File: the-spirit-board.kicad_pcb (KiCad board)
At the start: 4 copper layers, 25 x 43 mm, 60 parts, among them IC1 ESP32-C6-WROOM-1-N8, IC2 AP2112K-3.3TRG1, IC3 ICS-43434, J1 RAHUC31AUTR, Q1 BSS138, Q2 BSS138, Q3 BSS138, Q4 BSS138, Q5 BSS138, Q6 BSS138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

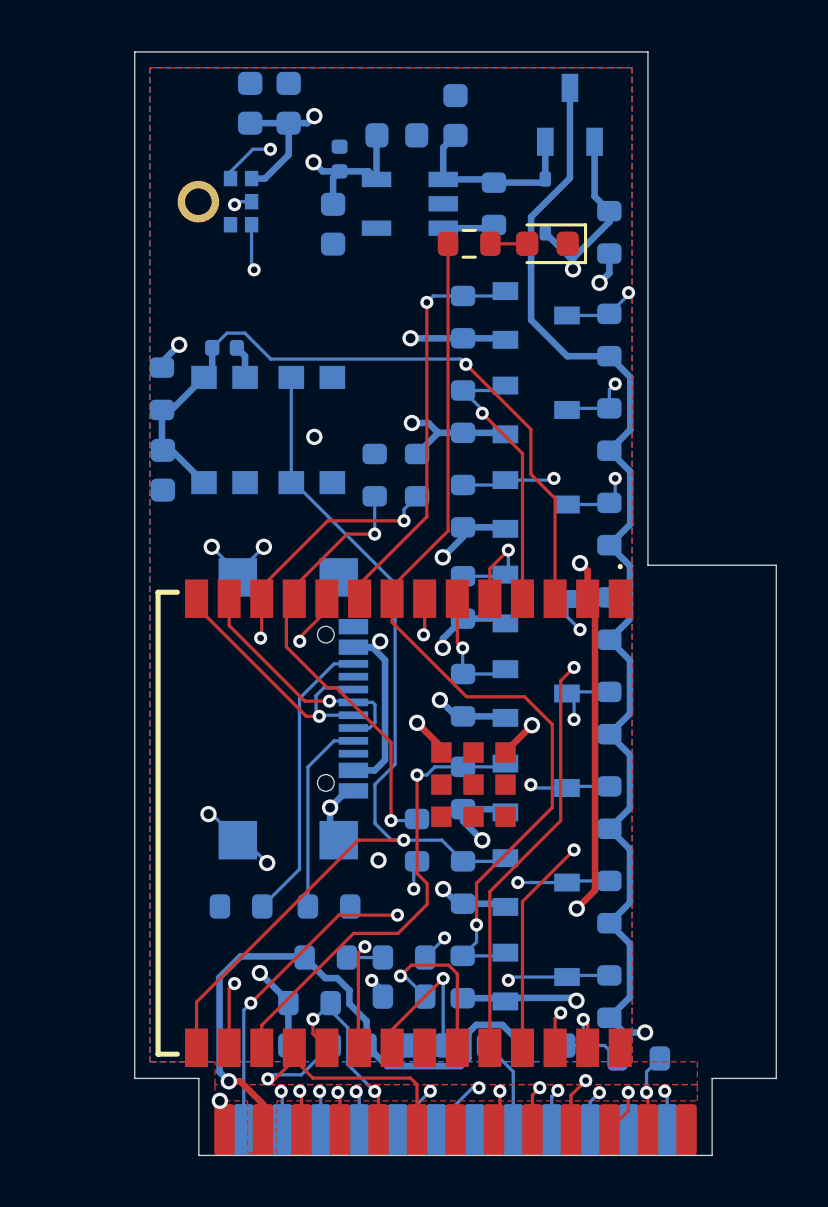
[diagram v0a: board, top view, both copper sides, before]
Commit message: Update the schematic and layout after choosing parts
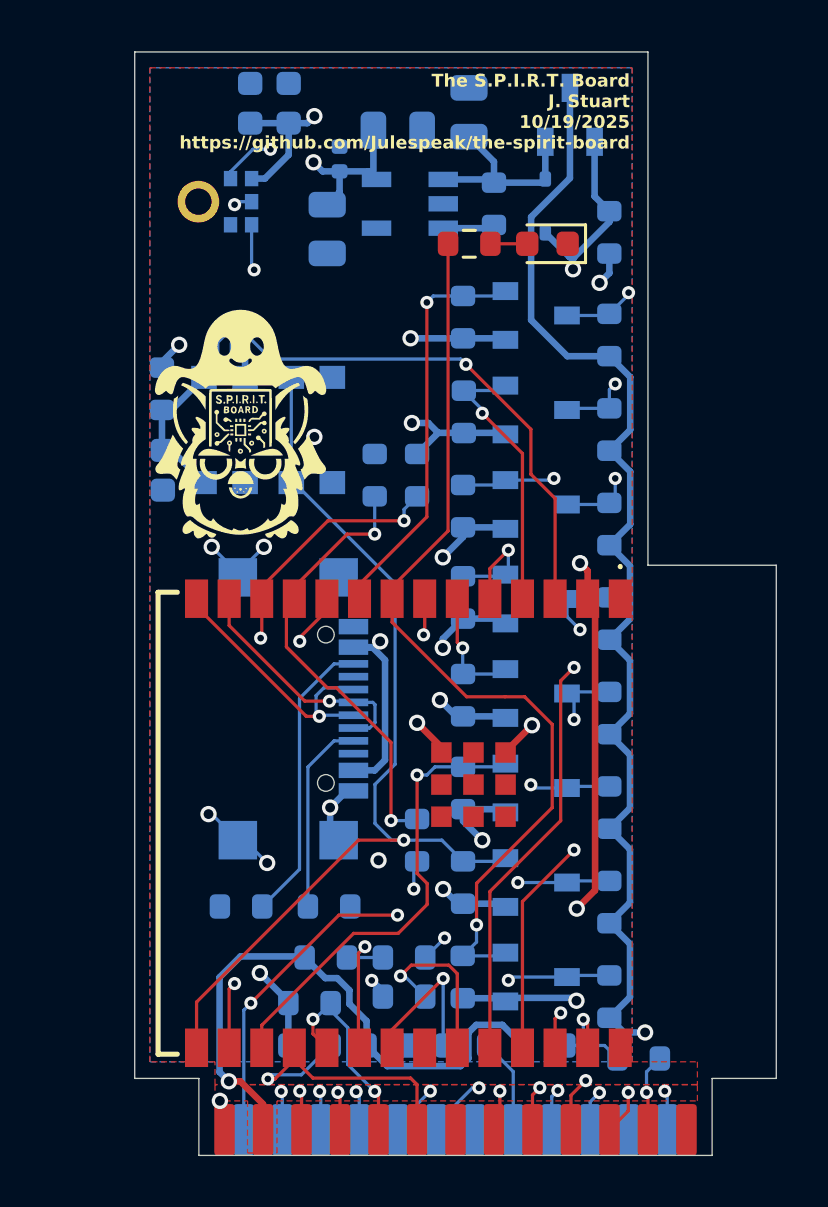
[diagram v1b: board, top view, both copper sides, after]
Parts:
- added G***: LOGO, TheSPIRITBoard:furby_logo, F.Cu at (144.1, 116.5)
- C4, C5, C6: footprint Capacitor_SMD:C_0603_1608Metric -> Capacitor_SMD:C_0805_2012Metric
- moved C5 0.54 mm to (153.0, 104.3)
- moved C4 0.30 mm to (147.5, 108.9)
- moved C6 0.20 mm to (150.2, 105.0)
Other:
- board text added: "BOOT"
- board text added: "EN"
- board text added: "The S.P.I.R.T. Board J. Stuart 10/19/2025 https://github.com/Julespeak/the-spirit-board"

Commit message: Update gerbers, BOM, and placement for JLCPCB
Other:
- board text added: "The S.P.I.R.I.T. Board J. Stuart 10/19/2025 https://github.com/Julespeak/the-spirit-board"
- board text removed: "The S.P.I.R.T. Board J. Stuart 10/19/2025 https://github.com/Julespeak/the-spirit-board"
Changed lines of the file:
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@@
 			(disableapertmacros no)
 			(usegerberextensions yes)
-			(usegerberattributes yes)
-			(usegerberadvancedattributes yes)
+			(usegerberattributes no)
+			(usegerberadvancedattributes no)
 			(creategerberjobfile yes)
 			(dashed_line_dash_ratio 12.000000)
@@
 			(sketchdnponfab yes)
 			(crossoutdnponfab yes)
-			(subtractmaskfromsilk no)
+			(subtractmaskfromsilk yes)
 			(outputformat 1)
 			(mirror no)
@@
 		)
 	)
-	(gr_text "The S.P.I.R.T. Board\nJ. Stuart\n10/19/2025\nhttps://github.com/Julespeak/the-spirit-board"
+	(gr_text "The S.P.I.R.I.T. Board\nJ. Stuart\n10/19/2025\nhttps://github.com/Julespeak/the-spirit-board"
 		(at 159.3 105.825 0)
 		(layer "F.SilkS")
